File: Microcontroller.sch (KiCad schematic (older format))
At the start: 15 parts, among them J6 Conn_01x06_Male, SW1 SW_Push, SW2 SW_Push, U2 PIC16F1939-IPT, Y1 Crystal

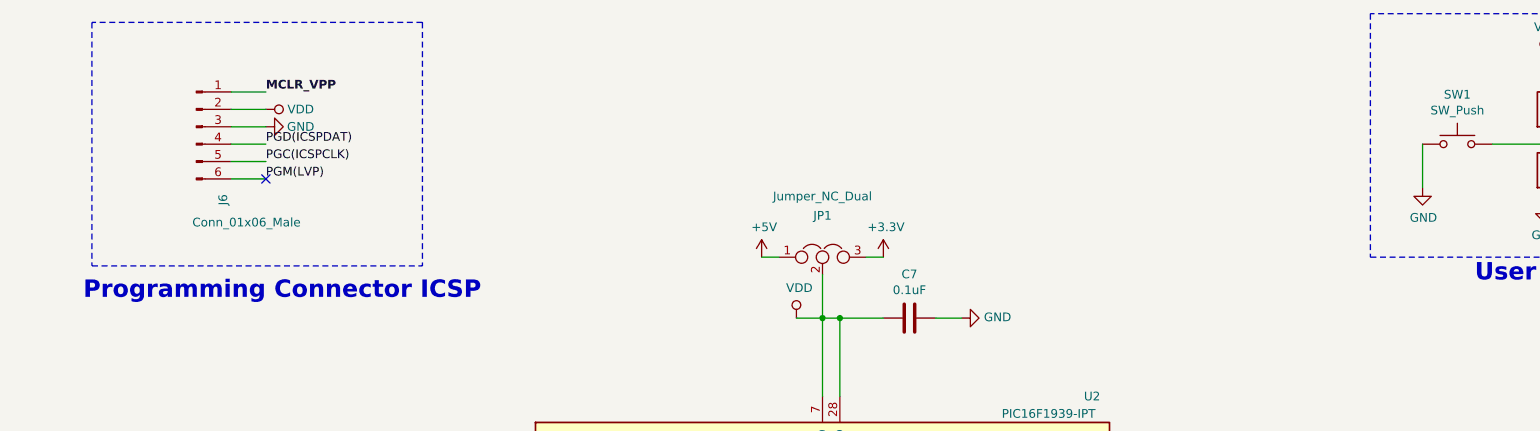
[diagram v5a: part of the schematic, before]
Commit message: Se agrega info del circuito,prolijidad en conexiones  se corrije,ERC Warninsg no errores,pendinete Datasheet y algunos numeros de parte,Comentario esquematico1: no es necesario con los labels que esta considero que esta ok, componentes los dejo en 0603, grilla en pcb 0.127 mm a criterio propio, se colocan fiduciales, pendiente lo demas de PCB.
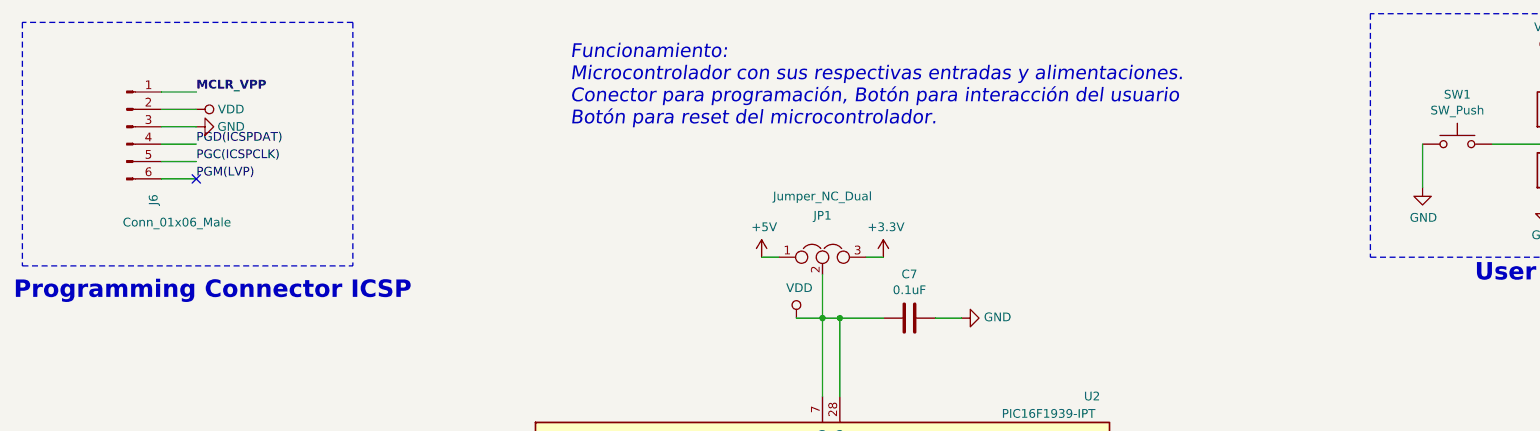
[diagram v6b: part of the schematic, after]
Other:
- note added: "Funcionamiento:\nMicrocontrolador con sus respectivas entradas y alimentaciones.\nConector para programación, Botón para interacción del usuario\nBotón para reset del microcontrolador."
- moved on the sheet: J6
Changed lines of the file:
@@
 Wire Wire Line
 	7500 3300 7850 3300
-$Comp
-L Connector:Conn_01x06_Male J6
-U 1 1 5CD0F49A
-P 2100 1450
-AR Path="/5CCEA06C/5CD0F49A" Ref="J6"  Part="1"
-AR Path="/5CFF2911/5CD0F49A" Ref="J?"  Part="1"
-AR Path="/5D021B48/5CD0F49A" Ref="J?"  Part="1"
-AR Path="/5D0426A9/5CD0F49A" Ref="J6"  Part="1"
-F 0 "J6" V 2254 1062 50  0000 R CNN
-F 1 "Conn_01x06_Male" H 2700 900 50  0000 R CNN
-F 2 "Connector_PinSocket_2.54mm:PinSocket_1x06_P2.54mm_Vertical" H 2100 1450 50  0001 C CNN
-F 3 "~" H 2100 1450 50  0001 C CNN
-	1    2100 1450
-	1    0    0    -1
-$EndComp
-Wire Wire Line
-	2300 1250 2500 1250
-Wire Wire Line
-	2300 1350 2500 1350
-Wire Wire Line
-	2300 1450 2500 1450
-Wire Wire Line
-	2300 1550 2500 1550
-Wire Wire Line
-	2500 1650 2300 1650
-Wire Wire Line
-	2300 1750 2500 1750
-Text Label 2500 1750 0    50   ~ 0
-PGM(LVP)
-Text Label 2500 1650 0    50   ~ 0
-PGC(ICSPCLK)
-Text Label 2500 1550 0    50   ~ 0
-PGD(ICSPDAT)
-Text Label 2500 1250 0    50   ~ 10
-MCLR_VPP
 Text Label 3700 5700 2    50   ~ 0
 PGD(ICSPDAT)
@@
 Text Notes 9450 2350 0    100  ~ 20
 User Button
-Text Notes 1450 2450 0    100  ~ 20
-Programming Connector ICSP
-Wire Notes Line width 20
-	3400 850  3400 2250
-Wire Notes Line width 20
-	1500 850  1500 2250
-Wire Notes Line width 20
-	3400 850  1500 850
-Wire Notes Line width 20
-	1500 2250 3400 2250
 Text Notes 9500 4500 0    100  ~ 20
 Reset Button
@@
 	1    0    0    -1
 $EndComp
-$Comp
-L power:VDD #PWR0114
-U 1 1 5CF4A32A
-P 2500 1350
-AR Path="/5CCEA06C/5CF4A32A" Ref="#PWR0114"  Part="1"
-AR Path="/5CFF2911/5CF4A32A" Ref="#PWR?"  Part="1"
-AR Path="/5D021B48/5CF4A32A" Ref="#PWR?"  Part="1"
-AR Path="/5D0426A9/5CF4A32A" Ref="#PWR011"  Part="1"
-F 0 "#PWR011" H 2500 1200 50  0001 C CNN
-F 1 "VDD" V 2500 1550 50  0000 C CNN
-F 2 "" H 2500 1350 50  0001 C CNN
-F 3 "" H 2500 1350 50  0001 C CNN
-	1    2500 1350
-	0    1    1    0
-$EndComp
-$Comp
-L power:GND #PWR0115
-U 1 1 5CF4CE26
-P 2500 1450
-AR Path="/5CCEA06C/5CF4CE26" Ref="#PWR0115"  Part="1"
-AR Path="/5CFF2911/5CF4CE26" Ref="#PWR?"  Part="1"
-AR Path="/5D021B48/5CF4CE26" Ref="#PWR?"  Part="1"
-AR Path="/5D0426A9/5CF4CE26" Ref="#PWR012"  Part="1"
-F 0 "#PWR012" H 2500 1200 50  0001 C CNN
-F 1 "GND" V 2500 1250 50  0000 C CNN
-F 2 "" H 2500 1450 50  0001 C CNN
-F 3 "" H 2500 1450 50  0001 C CNN
-	1    2500 1450
-	0    -1   -1   0
-$EndComp
 NoConn ~ 3900 4200
 Wire Wire Line
@@
 Wire Wire Line
 	5800 2550 6050 2550
-NoConn ~ 2500 1750
 Wire Wire Line
 	5550 2550 5700 2550
@@
 Wire Wire Line
 	9850 4800 9850 5050
-Wire Wire Line
-	5700 5800 5700 6050
 $Comp
 L power:GND #PWR0121
@@
 Wire Wire Line
 	5850 5800 5850 6050
+Wire Wire Line
+	5700 5800 5700 6050
+Text Notes 4250 1450 0    79   Italic 0
+Funcionamiento:\nMicrocontrolador con sus respectivas entradas y alimentaciones.\nConector para programación, Botón para interacción del usuario\nBotón para reset del microcontrolador.
+NoConn ~ 2100 1750
+$Comp
+L power:GND #PWR0115
+U 1 1 5CF4CE26
+P 2100 1450
+AR Path="/5CCEA06C/5CF4CE26" Ref="#PWR0115"  Part="1"
+AR Path="/5CFF2911/5CF4CE26" Ref="#PWR?"  Part="1"
+AR Path="/5D021B48/5CF4CE26" Ref="#PWR?"  Part="1"
+AR Path="/5D0426A9/5CF4CE26" Ref="#PWR012"  Part="1"
+F 0 "#PWR012" H 2100 1200 50  0001 C CNN
+F 1 "GND" V 2100 1250 50  0000 C CNN
+F 2 "" H 2100 1450 50  0001 C CNN
+F 3 "" H 2100 1450 50  0001 C CNN
+	1    2100 1450
+	0    -1   -1   0
+$EndComp
+$Comp
+L power:VDD #PWR0114
+U 1 1 5CF4A32A
+P 2100 1350
+AR Path="/5CCEA06C/5CF4A32A" Ref="#PWR0114"  Part="1"
+AR Path="/5CFF2911/5CF4A32A" Ref="#PWR?"  Part="1"
+AR Path="/5D021B48/5CF4A32A" Ref="#PWR?"  Part="1"
+AR Path="/5D0426A9/5CF4A32A" Ref="#PWR011"  Part="1"
+F 0 "#PWR011" H 2100 1200 50  0001 C CNN
+F 1 "VDD" V 2100 1550 50  0000 C CNN
+F 2 "" H 2100 1350 50  0001 C CNN
+F 3 "" H 2100 1350 50  0001 C CNN
+	1    2100 1350
+	0    1    1    0
+$EndComp
+Wire Notes Line width 20
+	1100 2250 3000 2250
+Wire Notes Line width 20
+	3000 850  1100 850
+Wire Notes Line width 20
+	1100 850  1100 2250
+Wire Notes Line width 20
+	3000 850  3000 2250
+Text Notes 1050 2450 0    100  ~ 20
+Programming Connector ICSP
+Text Label 2100 1250 0    50   ~ 10
+MCLR_VPP
+Text Label 2100 1550 0    50   ~ 0
+PGD(ICSPDAT)
+Text Label 2100 1650 0    50   ~ 0
+PGC(ICSPCLK)
+Text Label 2100 1750 0    50   ~ 0
+PGM(LVP)
+Wire Wire Line
+	1900 1750 2100 1750
+Wire Wire Line
+	2100 1650 1900 1650
+Wire Wire Line
+	1900 1550 2100 1550
+Wire Wire Line
+	1900 1450 2100 1450
+Wire Wire Line
+	1900 1350 2100 1350
+Wire Wire Line
+	1900 1250 2100 1250
+$Comp
+L Connector:Conn_01x06_Male J6
+U 1 1 5CD0F49A
+P 1700 1450
+AR Path="/5CCEA06C/5CD0F49A" Ref="J6"  Part="1"
+AR Path="/5CFF2911/5CD0F49A" Ref="J?"  Part="1"
+AR Path="/5D021B48/5CD0F49A" Ref="J?"  Part="1"
+AR Path="/5D0426A9/5CD0F49A" Ref="J6"  Part="1"
+F 0 "J6" V 1854 1062 50  0000 R CNN
+F 1 "Conn_01x06_Male" H 2300 900 50  0000 R CNN
+F 2 "Connector_PinSocket_2.54mm:PinSocket_1x06_P2.54mm_Vertical" H 1700 1450 50  0001 C CNN
+F 3 "~" H 1700 1450 50  0001 C CNN
+	1    1700 1450
+	1    0    0    -1
+$EndComp
 $EndSCHEMATC

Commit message: Se agrega reglas de pcb , se corrige ERC en sch, se agrega grilla 0.127(5 mils) , se agrega plano de tierra, keep out para perforaciones, se agrega rotulo , se rutea pocas pistas
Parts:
- removed U2: PIC16F1939-IPT, Package_QFP:TQFP-44_10x10mm_P0.8mm, symbol MCU_Microchip_PIC16:PIC16F1939-IPT
- added U2: PIC16F1934-IPT_J, symbol MCU_Microchip_PIC16_Updtate:PIC16F1934-IPT_J
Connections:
- net GND: now also U2.29 (VSS), U2.6 (VSS)
- net LED_B: now also U2.27 (SEG23/CCP5/AN7/RE2)
- net LED_G: now also U2.26 (SEG22/P3B/AN6/RE1)
- net LED_OUT: now also U2.32 (P2B/T1CKI/T1OSO/RC0)
- net LED_R: now also U2.25 (SEG21/P3A/CCP3/AN5/RE0)
- net MCLR_VPP: now also U2.18 (RE3/MCLR/Vpp)
- net POT_AN5: now also U2.24 (RA5/AN4/C2OUT/CPS7/SRNQ/SS/VCAP/SEG5)
- net RA0_AN0: now also U2.19 (RA0/AN0/C12IN0-/C2OUT/SRNQ/SS/VCAP/SEG12)
- net RA1_AN1: now also U2.20 (RA1/AN1/C12IN1-/SEG7)
- net RA2_AN2: now also U2.21 (RA2/AN2/C2IN+/Vref-/DACOUT/COM2)
- net RA3_AN3: now also U2.22 (RA3/AN3/C1IN+/Vref+/SEG15)
- net RB1: now also U2.9 (RB1/AN10/C12IN3-/CPS1/VLCD1)
- net RB2: now also U2.10 (RB2/AN8/CPS2/VLCD2)
- net RB3: now also U2.11 (RB3/AN9/C12IN2-/CPS3/CCP2/P2A/VLCD3)
- net RB4: now also U2.14 (RB4/AN11/CPS4/COM0)
- net RB5: now also U2.15 (RB5/AN13/CPS5/CCP3/P3A/T1G/COM1)
- net RB6: now also U2.16 (RB6/ICSPCLK/ICDCLK/SEG14)
- net RB7: now also U2.17 (RB7/ICSPDAT/ICDDAT/SEG13)
- net RC1: now also U2.35 (P2A/CCP2/T1OSI/RC1)
- net RC2: now also U2.36 (SEG3/P1A/CCP1/RC2)
- net RC5: now also U2.43 (SEG10/SDO/RC5)
- net RD0: now also U2.38 (COM3/CPS8/RD0)
- net RD1: now also U2.39 (CCP4/CPS9/RD1)
- net RD2: now also U2.40 (P2B/CPS10/RD2)
- net RD3: now also U2.41 (SEG16/P2C/CPS11/RD3)
- net RD4: now also U2.2 (SEG17/P2D/CPS12/RD4)
- net RD5: now also U2.3 (SEG18/P1B/CPS13/RD5)
- net RD6: now also U2.4 (SEG19/P1C/CPS14/RD6)
- net RD7: now also U2.5 (SEG20/P1D/CPS15/RD7)
- net SCL_I2C: now also U2.42 (SEG11/T1G/SDA/SDI/RC4)
- net SDA_I2C: now also U2.37 (SEG6/SCLK/SCL/RC3)
- net USER_BUTTON: now also U2.8 (RB0/AN12/CPS0/SRI/INT/SEG0)
- net VDD: now also U2.28 (VDD), U2.7 (VDD)
- net at R2.1: now also U2.1 (SEG8/DT/RX/RC7)
- net at C6.2, Y1.1: now also U2.30 (RA7/OSC1/CLKIN/SEG2)
- net at C5.2, Y1.2: now also U2.31 (RA6/OSC2/CLKOUT/VCAP/SEG1)
- net at R1.1: now also U2.44 (SEG9/CK/TX/RC6)
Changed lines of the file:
@@
 	0    -1   -1   0
 $EndComp
-Wire Wire Line
-	6350 2550 6500 2550
 $Comp
 L Device:Crystal Y1
@@
 	5700 2300 5700 2550
 Connection ~ 5700 2550
-Wire Wire Line
-	5700 2550 5700 3000
 $Comp
 L Device:C C7
@@
 L power:GND #PWR013
 U 1 1 5CD587E3
-P 9850 1900
+P 9850 2000
 AR Path="/5CCEA06C/5CD587E3" Ref="#PWR013"  Part="1"
 AR Path="/5CFF2911/5CD587E3" Ref="#PWR?"  Part="1"
 AR Path="/5D021B48/5CD587E3" Ref="#PWR?"  Part="1"
 AR Path="/5D0426A9/5CD587E3" Ref="#PWR026"  Part="1"
-F 0 "#PWR026" H 9850 1650 50  0001 C CNN
-F 1 "GND" H 9855 1727 50  0000 C CNN
-F 2 "" H 9850 1900 50  0001 C CNN
-F 3 "" H 9850 1900 50  0001 C CNN
-	1    9850 1900
-	1    0    0    -1
-$EndComp
-Wire Wire Line
-	9850 1850 9850 1900
+F 0 "#PWR026" H 9850 1750 50  0001 C CNN
+F 1 "GND" H 9855 1827 50  0000 C CNN
+F 2 "" H 9850 2000 50  0001 C CNN
+F 3 "" H 9850 2000 50  0001 C CNN
+	1    9850 2000
+	1    0    0    -1
+$EndComp
 Text Label 10000 1550 0    50   ~ 10
 USER_BUTTON
@@
 Text HLabel 7850 3300 2    50   Output ~ 10
 LED_OUT
-$Comp
-L MCU_Microchip_PIC16:PIC16F1939-IPT U2
-U 1 1 5CCEA30F
-P 5700 4400
-AR Path="/5CCEA06C/5CCEA30F" Ref="U2"  Part="1"
-AR Path="/5CFF2911/5CCEA30F" Ref="U?"  Part="1"
-AR Path="/5D021B48/5CCEA30F" Ref="U?"  Part="1"
-AR Path="/5D0426A9/5CCEA30F" Ref="U2"  Part="1"
-F 0 "U2" H 7250 5800 50  0000 C CNN
-F 1 "PIC16F1939-IPT" H 7000 5700 50  0000 C CNN
-F 2 "Package_QFP:TQFP-44_10x10mm_P0.8mm" H 5700 4400 50  0001 C CNN
-F 3 "http://ww1.microchip.com/downloads/en/DeviceDoc/41364E.pdf" H 5700 4400 50  0001 C CNN
-	1    5700 4400
-	1    0    0    -1
-$EndComp
 Text HLabel 3700 5550 0    50   Output ~ 10
 RB7
@@
 	1    0    0    -1
 $EndComp
+Wire Wire Line
+	9850 1850 9850 2000
+$Comp
+L MCU_Microchip_PIC16_Updtate:PIC16F1934-IPT_J U2
+U 1 1 5D05B785
+P 5700 4400
+F 0 "U2" H 7300 5700 50  0000 C CNN
+F 1 "PIC16F1934-IPT_J" H 4400 5700 50  0000 C CNN
+F 2 "" H 5700 4400 50  0001 C CNN
+F 3 "http://ww1.microchip.com/downloads/en/DeviceDoc/41364E.pdf" H 5700 4400 50  0001 C CNN
+	1    5700 4400
+	1    0    0    -1
+$EndComp
+Wire Wire Line
+	6400 2550 6500 2550
+Wire Wire Line
+	6350 2550 6400 2550
+Connection ~ 6400 2550
+Wire Wire Line
+	6400 2700 6400 2550
+$Comp
+L power:PWR_FLAG #FLG0102
+U 1 1 5D04333F
+P 6400 2700
+F 0 "#FLG0102" H 6400 2775 50  0001 C CNN
+F 1 "PWR_FLAG" H 6400 2873 50  0000 C CNN
+F 2 "" H 6400 2700 50  0001 C CNN
+F 3 "~" H 6400 2700 50  0001 C CNN
+	1    6400 2700
+	-1   0    0    1
+$EndComp
+Connection ~ 5700 2750
+Wire Wire Line
+	5700 2750 5700 3000
+Wire Wire Line
+	5700 2550 5700 2750
+Wire Wire Line
+	5550 2750 5700 2750
+$Comp
+L power:PWR_FLAG #FLG0101
+U 1 1 5D032492
+P 5550 2750
+F 0 "#FLG0101" H 5550 2825 50  0001 C CNN
+F 1 "PWR_FLAG" V 5550 2877 50  0000 L CNN
+F 2 "" H 5550 2750 50  0001 C CNN
+F 3 "~" H 5550 2750 50  0001 C CNN
+	1    5550 2750
+	0    -1   -1   0
+$EndComp
 $EndSCHEMATC

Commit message: Se agregan cosas obligatorias por norma y algunas sugerencias por el docente
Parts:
- U2: symbol MCU_Microchip_PIC16_Updtate:PIC16F1934-IPT_J -> TPDSI_1-rescue:PIC16F1934-IPT_J-MCU_Microchip_PIC16_Updtate
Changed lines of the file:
@@
 	9850 1850 9850 2000
 $Comp
-L MCU_Microchip_PIC16_Updtate:PIC16F1934-IPT_J U2
+L TPDSI_1-rescue:PIC16F1934-IPT_J-MCU_Microchip_PIC16_Updtate U2
 U 1 1 5D05B785
 P 5700 4400
+AR Path="/5D05B785" Ref="U2"  Part="1"
+AR Path="/5D0426A9/5D05B785" Ref="U2"  Part="1"
 F 0 "U2" H 7300 5700 50  0000 C CNN
 F 1 "PIC16F1934-IPT_J" H 4400 5700 50  0000 C CNN
